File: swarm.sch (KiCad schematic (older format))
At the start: 25 parts, among them P1 USB_OTG, P2 CONN_01X05, P3 CONN_02X20, SW1 SW_PUSH, U1 LM3671MF-3.3, U2 STM32F103RETx, U3 APA102, Y1 Crystal

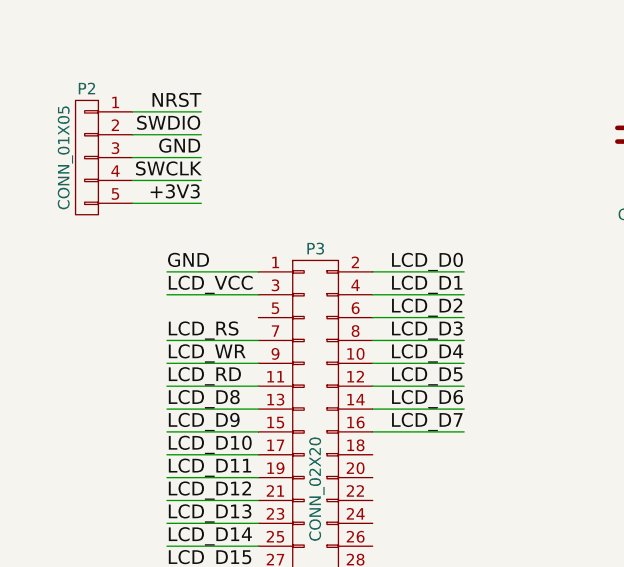
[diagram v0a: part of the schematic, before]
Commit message: Sime very important changes Connect LCD_VCC pin to VCC net, this was previously not connected Makes all elements (tracks and vias) in Power net compliant with its constraints
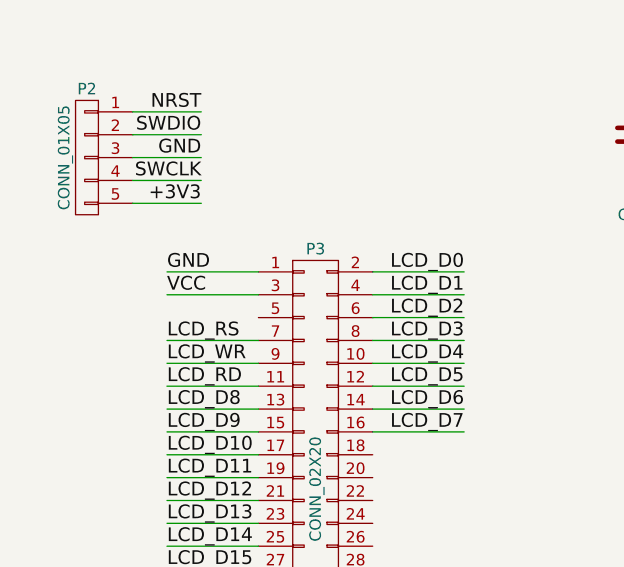
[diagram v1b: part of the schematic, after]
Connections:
- net LCD_VCC is gone; now on net VCC: P3.3 (P3)
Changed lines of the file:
@@
 GND
 Text Label 1300 5250 0    60   ~ 0
-LCD_VCC
+VCC
 Text Label 1300 5450 0    60   ~ 0
 LCD_RS

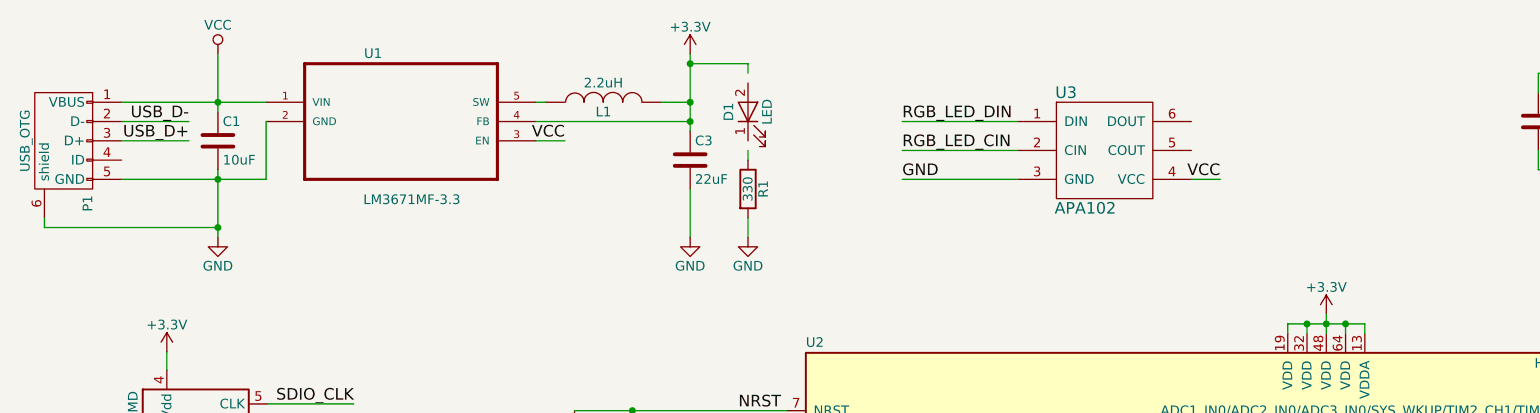
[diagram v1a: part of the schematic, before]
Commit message: Adds fuse (MF-PSMF050X) to schematic and layout
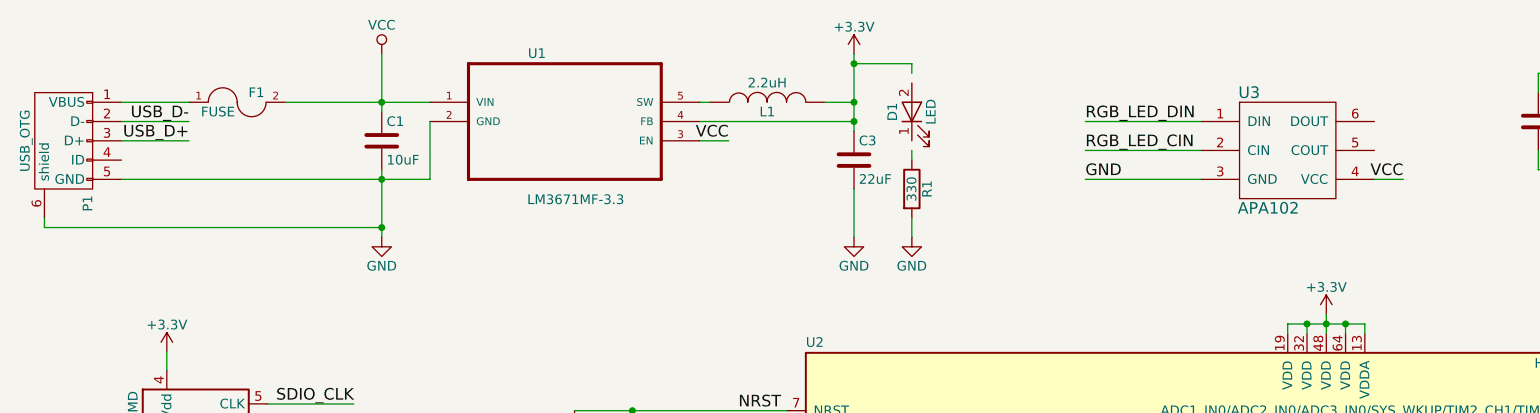
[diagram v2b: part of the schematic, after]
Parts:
- added F1: FUSE, volium:MF-PSMF050X, symbol FUSE
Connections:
- net VCC: now also F1.2; no longer P1.1 (VBUS)
- new net: F1.1, P1.1 (VBUS)
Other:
- moved on the sheet: C1, C3, D1, L1, R1, U1, U3

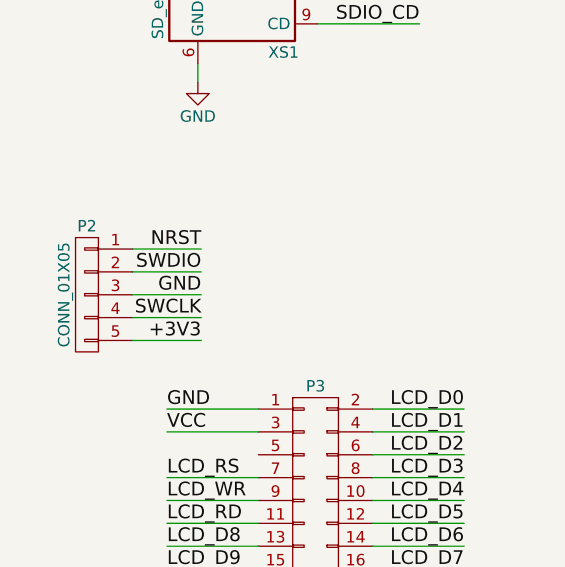
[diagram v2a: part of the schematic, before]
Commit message: Fixes pinout of debug connector, still needs to reroute
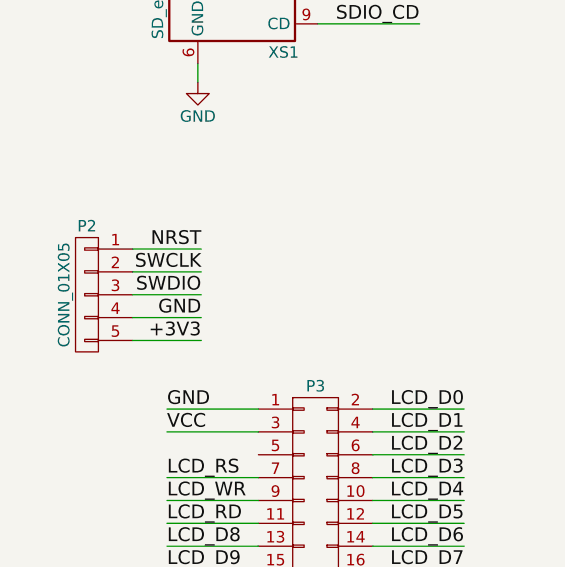
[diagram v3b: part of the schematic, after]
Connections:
- net GND: now also P2.4 (P4); no longer P2.3 (P3)
- net SWCLK: now also P2.2 (P2); no longer P2.4 (P4)
- net SWDIO: now also P2.3 (P3); no longer P2.2 (P2)
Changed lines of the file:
@@
 $EndComp
 Text Label 1450 4550 2    60   ~ 0
+SWCLK
+Text Label 1450 4650 2    60   ~ 0
 SWDIO
-Text Label 1450 4650 2    60   ~ 0
+Text Label 1450 4750 2    60   ~ 0
 GND
-Text Label 1450 4750 2    60   ~ 0
-SWCLK
 Text Label 1450 4850 2    60   ~ 0
 +3V3

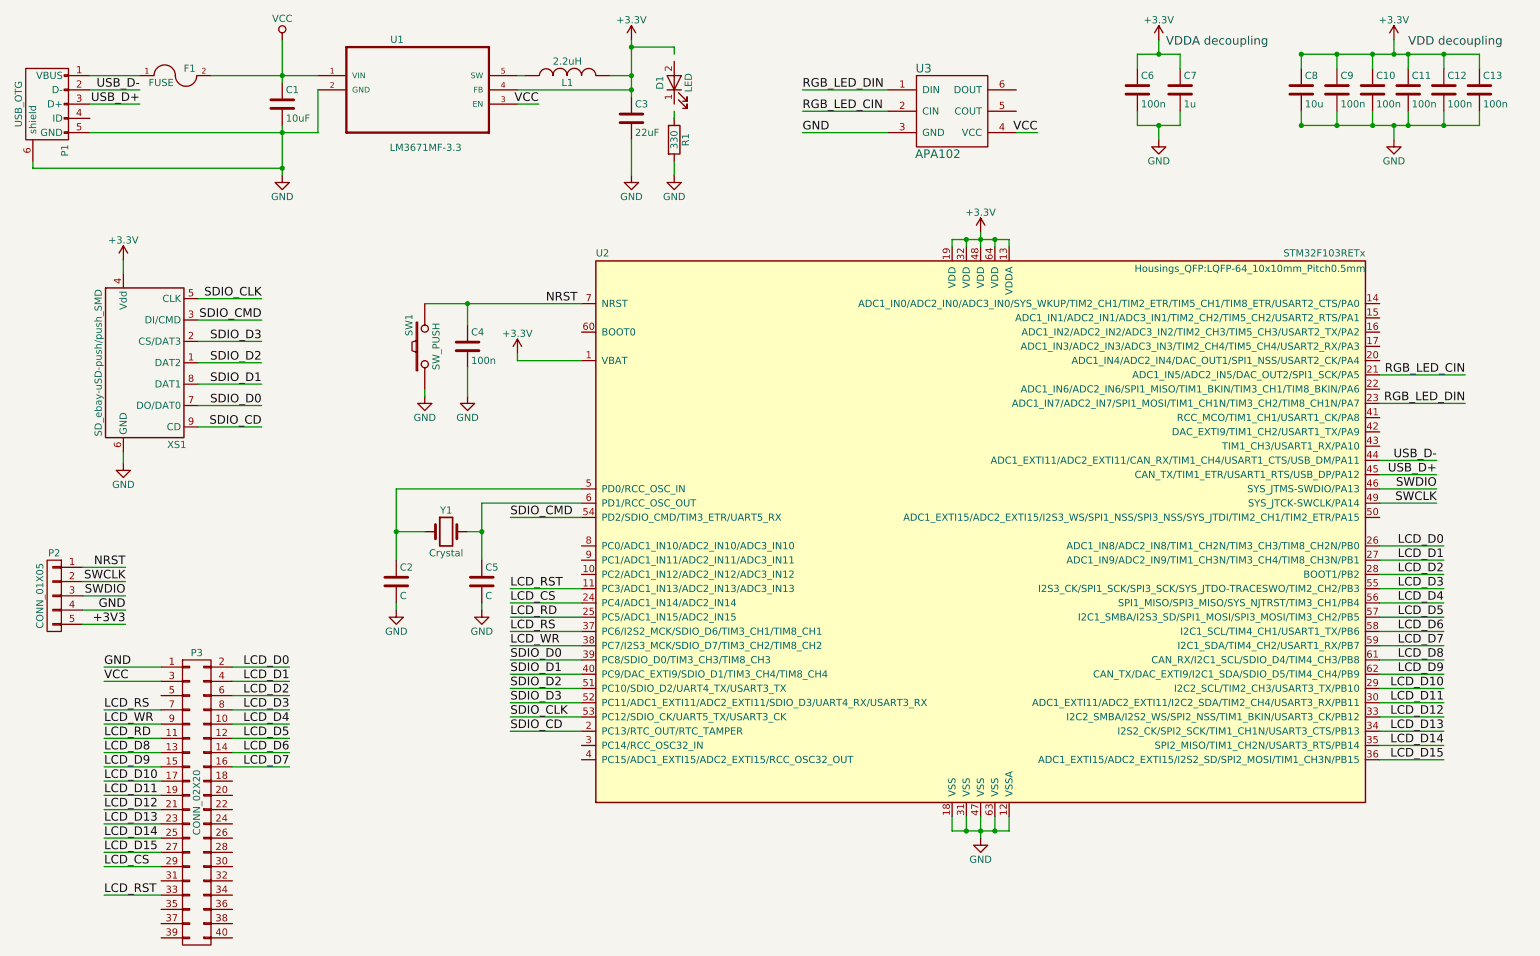
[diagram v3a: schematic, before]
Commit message: Adds LED to TIM2_CH1 (pin 50) Added PWR label, cleanup
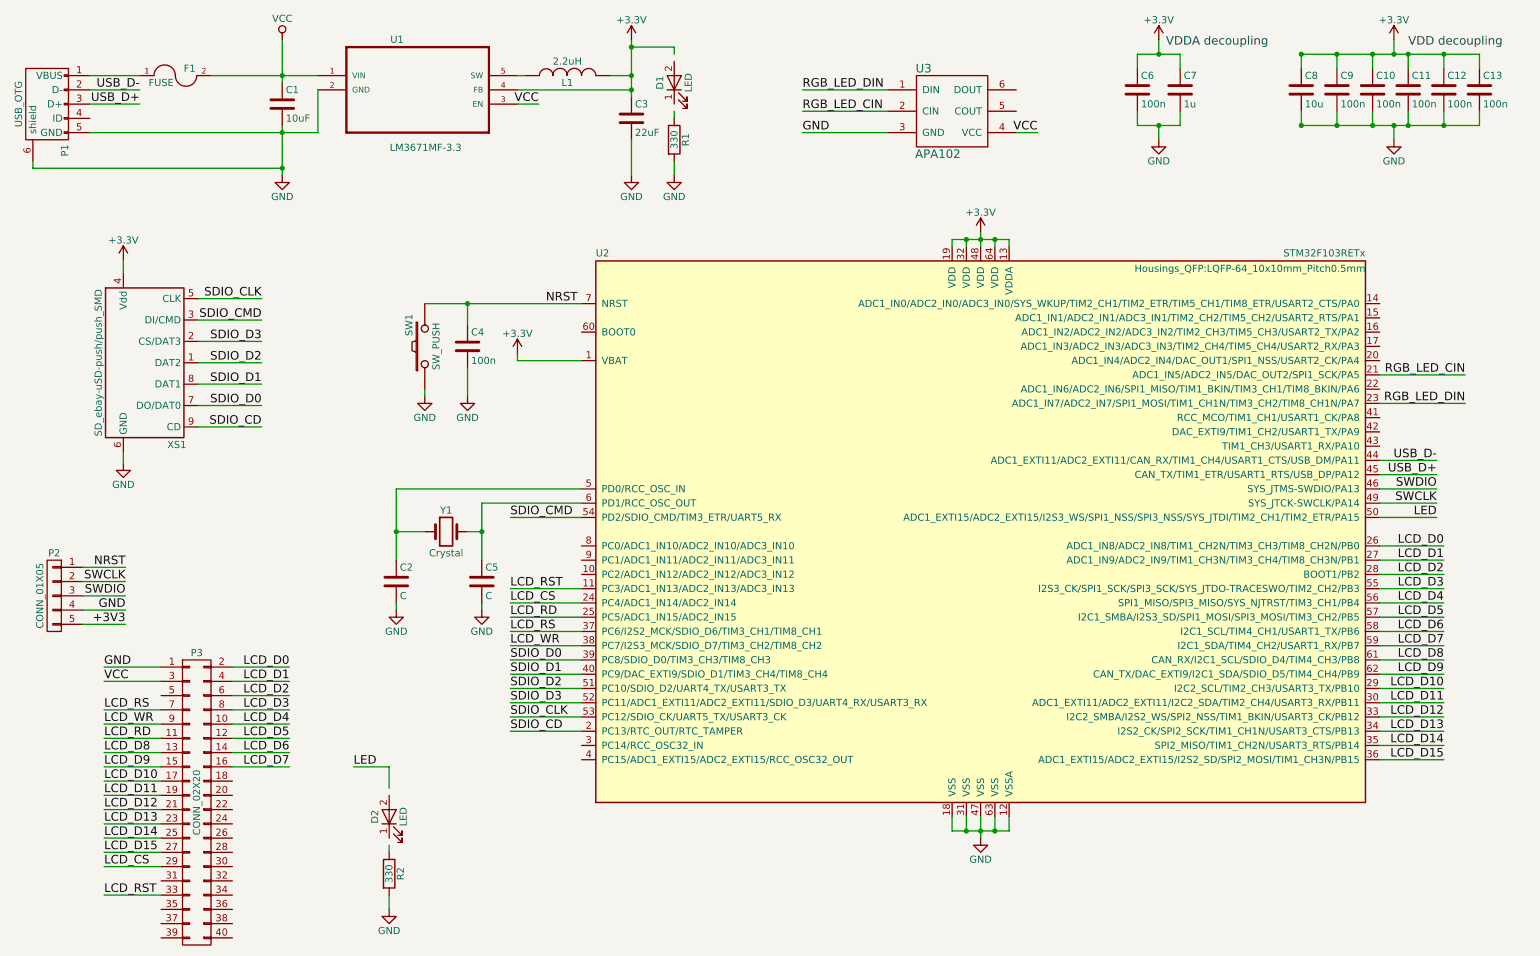
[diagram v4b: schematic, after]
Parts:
- added D2: LED, LEDs:LED_0805, symbol LED
- added R2: 330, Resistors_SMD:R_0805, symbol R
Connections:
- net GND: now also R2.2
- net LED: now reaches U2.50 (ADC1_EXTI15/ADC2_EXTI15/I2S3_WS/SPI1_NSS/SPI3_NSS/SYS_JTDI/TIM2_CH1/TIM2_ETR/PA15)
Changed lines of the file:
@@
 Wire Wire Line
 	1200 1000 1550 1000
+Text Label 10650 4100 2    60   ~ 0
+LED
+$Comp
+L LED D2
+U 1 1 5855C677
+P 3300 6200
+F 0 "D2" H 3300 6300 50  0000 C CNN
+F 1 "LED" H 3300 6100 50  0000 C CNN
+F 2 "LEDs:LED_0805" H 3300 6200 50  0001 C CNN
+F 3 "" H 3300 6200 50  0000 C CNN
+	1    3300 6200
+	0    -1   -1   0
+$EndComp
+$Comp
+L GND #PWR019
+U 1 1 5855C67D
+P 3300 6850
+F 0 "#PWR019" H 3300 6600 50  0001 C CNN
+F 1 "GND" H 3300 6700 50  0000 C CNN
+F 2 "" H 3300 6850 50  0000 C CNN
+F 3 "" H 3300 6850 50  0000 C CNN
+	1    3300 6850
+	1    0    0    -1
+$EndComp
+$Comp
+L R R2
+U 1 1 5855C683
+P 3300 6600
+F 0 "R2" V 3380 6600 50  0000 C CNN
+F 1 "330" V 3300 6600 50  0000 C CNN
+F 2 "Resistors_SMD:R_0805" V 3230 6600 50  0001 C CNN
+F 3 "" H 3300 6600 50  0000 C CNN
+	1    3300 6600
+	1    0    0    -1
+$EndComp
+Wire Wire Line
+	3300 6400 3300 6450
+Wire Wire Line
+	3300 6750 3300 6850
+Wire Wire Line
+	3300 6000 3300 5850
+Wire Wire Line
+	3300 5850 3050 5850
+Text Label 3050 5850 0    60   ~ 0
+LED
+Wire Wire Line
+	10250 4100 10650 4100
 $EndSCHEMATC

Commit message: Updates after upgrading to KiCAD 4.0.5 Updated schematic components to new libraries Cleaned up some tracks in layout
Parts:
- F1: symbol FUSE -> Polyfuse
- L1: symbol INDUCTOR -> L
- SW1: symbol SW_PUSH -> SW_Push
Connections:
- net +3V3: now also D1.2 (A)
- net LED: now also D2.2 (A)
- net at D1.1 (K): now also R1.1
- net at D2.1 (K): now also R2.1
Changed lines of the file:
@@
 LIBS:stm32
 LIBS:volium
+LIBS:switches
 LIBS:swarm-cache
 EELAYER 25 0
@@
 $EndComp
 $Comp
-L SW_PUSH SW1
+L SW_Push SW1
 U 1 1 5813891F
 P 3550 2900
@@
 $EndComp
 $Comp
-L INDUCTOR L1
+L L L1
 U 1 1 5840B3E5
 P 4550 1000
@@
 SDIO_CD
 $Comp
-L FUSE F1
+L Polyfuse F1
 U 1 1 584EF4C4
 P 1800 1000
-F 0 "F1" H 1900 1050 50  0000 C CNN
-F 1 "FUSE" H 1700 950 50  0000 C CNN
+F 0 "F1" V 1900 1050 50  0000 C CNN
+F 1 "FUSE" V 1700 950 50  0000 C CNN
 F 2 "volium:MF-PSMF050X" H 1800 1000 50  0001 C CNN
 F 3 "" H 1800 1000 50  0000 C CNN
 	1    1800 1000
-	1    0    0    -1
+	0    -1   -1   0
 $EndComp
 Wire Wire Line
@@
 Connection ~ 7450 6300
 Wire Wire Line
-	7450 6200 7450 6350
+	7450 6200 7450 6300
+Wire Wire Line
+	7450 6300 7450 6350
 Connection ~ 7450 2150
 Wire Wire Line
@@
 Connection ~ 7550 2150
 Wire Wire Line
-	7450 2100 7450 2200
+	7450 2100 7450 2150
+Wire Wire Line
+	7450 2150 7450 2200
 Wire Wire Line
 	7350 2200 7350 2150
@@
 	7250 2150 7250 2200
 Wire Wire Line
-	7250 6300 7650 6300
+	7250 6300 7350 6300
+Wire Wire Line
+	7350 6300 7450 6300
+Wire Wire Line
+	7450 6300 7550 6300
+Wire Wire Line
+	7550 6300 7650 6300
 Wire Wire Line
 	7650 6300 7650 6200
@@
 Connection ~ 10350 850
 Wire Wire Line
-	9700 1350 10950 1350
+	9700 1350 9950 1350
+Wire Wire Line
+	9950 1350 10200 1350
+Wire Wire Line
+	10200 1350 10350 1350
+Wire Wire Line
+	10350 1350 10450 1350
+Wire Wire Line
+	10450 1350 10700 1350
+Wire Wire Line
+	10700 1350 10950 1350
 Wire Wire Line
 	10700 1350 10700 1250
@@
 	3850 3050 3850 3250
 Wire Wire Line
-	3550 2600 4650 2600
+	3550 2600 3850 2600
+Wire Wire Line
+	3850 2600 4650 2600
 Wire Wire Line
 	3850 2600 3850 2750
 Wire Wire Line
-	3550 3250 3550 3200
+	3550 3250 3550 3100
 Connection ~ 3850 2600
 Wire Wire Line
 	4650 3900 3350 3900
 Wire Wire Line
-	3350 3900 3350 4400
+	3350 3900 3350 4200
+Wire Wire Line
+	3350 4200 3350 4400
 Wire Wire Line
 	3350 4200 3550 4200
@@
 	3850 4200 3950 4200
 Wire Wire Line
-	3950 4000 3950 4400
+	3950 4000 3950 4200
+Wire Wire Line
+	3950 4200 3950 4400
 Wire Wire Line
 	3950 4750 3950 4700
@@
 Connection ~ 2550 1000
 Wire Wire Line
-	2550 1350 2550 1700
-Wire Wire Line
-	1200 1400 2800 1400
-Wire Wire Line
-	5000 750  5000 1150
+	2550 1350 2550 1400
+Wire Wire Line
+	2550 1400 2550 1650
+Wire Wire Line
+	2550 1650 2550 1700
+Wire Wire Line
+	1200 1400 2550 1400
+Wire Wire Line
+	2550 1400 2800 1400
+Wire Wire Line
+	5000 750  5000 800
+Wire Wire Line
+	5000 800  5000 1000
+Wire Wire Line
+	5000 1000 5000 1100
+Wire Wire Line
+	5000 1100 5000 1150
 Wire Wire Line
 	4200 1100 5000 1100
 Wire Wire Line
-	2550 750  2550 1050
+	2550 750  2550 1000
+Wire Wire Line
+	2550 1000 2550 1050
 Connection ~ 5000 1000
 Wire Wire Line
@@
 	4200 1200 4350 1200
 Wire Wire Line
-	2050 1000 2800 1000
+	1950 1000 2550 1000
+Wire Wire Line
+	2550 1000 2800 1000
 Connection ~ 5000 1100
 Wire Wire Line
-	4850 1000 5000 1000
-Wire Wire Line
-	5300 800  5300 850
+	4700 1000 5000 1000
+Wire Wire Line
+	5300 800  5300 900
 Wire Wire Line
 	5000 800  5300 800
 Connection ~ 5000 800
 Wire Wire Line
-	5300 1250 5300 1300
+	5300 1200 5300 1300
 Wire Wire Line
 	5300 1600 5300 1700
 Connection ~ 2550 1400
 Wire Wire Line
-	4200 1000 4250 1000
+	4200 1000 4400 1000
 Wire Wire Line
 	10250 4300 10700 4300
@@
 	8550 1250 8550 1350
 Wire Wire Line
-	8550 1350 8850 1350
+	8550 1350 8700 1350
+Wire Wire Line
+	8700 1350 8850 1350
 Wire Wire Line
 	8850 1350 8850 1250
@@
 	8850 850  8850 950
 Wire Wire Line
-	8550 850  8850 850
+	8550 850  8700 850
+Wire Wire Line
+	8700 850  8850 850
 Wire Wire Line
 	8700 850  8700 750
@@
 	10250 3300 10850 3300
 Wire Wire Line
-	9700 850  10950 850
+	9700 850  9950 850
+Wire Wire Line
+	9950 850  10200 850
+Wire Wire Line
+	10200 850  10350 850
+Wire Wire Line
+	10350 850  10450 850
+Wire Wire Line
+	10450 850  10700 850
+Wire Wire Line
+	10700 850  10950 850
 Wire Wire Line
 	6800 1400 6200 1400
@@
 	10950 1350 10950 1250
 Wire Wire Line
-	7250 2150 7650 2150
+	7250 2150 7350 2150
+Wire Wire Line
+	7350 2150 7450 2150
+Wire Wire Line
+	7450 2150 7550 2150
+Wire Wire Line
+	7550 2150 7650 2150
 Wire Wire Line
 	7650 2150 7650 2200
@@
 	4650 5600 4150 5600
 Wire Wire Line
-	1200 1000 1550 1000
+	1200 1000 1650 1000
 Text Label 10650 4100 2    60   ~ 0
 LED
@@
 $EndComp
 Wire Wire Line
-	3300 6400 3300 6450
+	3300 6350 3300 6450
 Wire Wire Line
 	3300 6750 3300 6850
 Wire Wire Line
-	3300 6000 3300 5850
+	3300 6050 3300 5850
 Wire Wire Line
 	3300 5850 3050 5850
@@
 Wire Wire Line
 	10250 4100 10650 4100
+Wire Wire Line
+	3550 2600 3550 2700
 $EndSCHEMATC

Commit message: Minor changes
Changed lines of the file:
@@
 Connection ~ 7450 6300
 Wire Wire Line
-	7450 6200 7450 6300
-Wire Wire Line
-	7450 6300 7450 6350
+	7450 6200 7450 6350
 Connection ~ 7450 2150
 Wire Wire Line
@@
 Connection ~ 7550 2150
 Wire Wire Line
-	7450 2100 7450 2150
-Wire Wire Line
-	7450 2150 7450 2200
+	7450 2100 7450 2200
 Wire Wire Line
 	7350 2200 7350 2150
@@
 	7250 2150 7250 2200
 Wire Wire Line
-	7250 6300 7350 6300
-Wire Wire Line
-	7350 6300 7450 6300
-Wire Wire Line
-	7450 6300 7550 6300
-Wire Wire Line
-	7550 6300 7650 6300
+	7250 6300 7650 6300
 Wire Wire Line
 	7650 6300 7650 6200
@@
 Connection ~ 10350 850
 Wire Wire Line
-	9700 1350 9950 1350
-Wire Wire Line
-	9950 1350 10200 1350
-Wire Wire Line
-	10200 1350 10350 1350
-Wire Wire Line
-	10350 1350 10450 1350
-Wire Wire Line
-	10450 1350 10700 1350
-Wire Wire Line
-	10700 1350 10950 1350
+	9700 1350 10950 1350
 Wire Wire Line
 	10700 1350 10700 1250
@@
 	3850 3050 3850 3250
 Wire Wire Line
-	3550 2600 3850 2600
-Wire Wire Line
-	3850 2600 4650 2600
+	3550 2600 4650 2600
 Wire Wire Line
 	3850 2600 3850 2750
@@
 	4650 3900 3350 3900
 Wire Wire Line
-	3350 3900 3350 4200
-Wire Wire Line
-	3350 4200 3350 4400
+	3350 3900 3350 4400
 Wire Wire Line
 	3350 4200 3550 4200
@@
 	3850 4200 3950 4200
 Wire Wire Line
-	3950 4000 3950 4200
-Wire Wire Line
-	3950 4200 3950 4400
+	3950 4000 3950 4400
 Wire Wire Line
 	3950 4750 3950 4700
@@
 Connection ~ 2550 1000
 Wire Wire Line
-	2550 1350 2550 1400
-Wire Wire Line
-	2550 1400 2550 1650
-Wire Wire Line
-	2550 1650 2550 1700
-Wire Wire Line
-	1200 1400 2550 1400
-Wire Wire Line
-	2550 1400 2800 1400
-Wire Wire Line
-	5000 750  5000 800
-Wire Wire Line
-	5000 800  5000 1000
-Wire Wire Line
-	5000 1000 5000 1100
-Wire Wire Line
-	5000 1100 5000 1150
+	2550 1350 2550 1700
+Wire Wire Line
+	1200 1400 2800 1400
+Wire Wire Line
+	5000 750  5000 1150
 Wire Wire Line
 	4200 1100 5000 1100
 Wire Wire Line
-	2550 750  2550 1000
-Wire Wire Line
-	2550 1000 2550 1050
+	2550 750  2550 1050
 Connection ~ 5000 1000
 Wire Wire Line
@@
 	4200 1200 4350 1200
 Wire Wire Line
-	1950 1000 2550 1000
-Wire Wire Line
-	2550 1000 2800 1000
+	1950 1000 2800 1000
 Connection ~ 5000 1100
 Wire Wire Line
@@
 	8550 1250 8550 1350
 Wire Wire Line
-	8550 1350 8700 1350
-Wire Wire Line
-	8700 1350 8850 1350
+	8550 1350 8850 1350
 Wire Wire Line
 	8850 1350 8850 1250
@@
 	8850 850  8850 950
 Wire Wire Line
-	8550 850  8700 850
-Wire Wire Line
-	8700 850  8850 850
+	8550 850  8850 850
 Wire Wire Line
 	8700 850  8700 750
@@
 	10250 3300 10850 3300
 Wire Wire Line
-	9700 850  9950 850
-Wire Wire Line
-	9950 850  10200 850
-Wire Wire Line
-	10200 850  10350 850
-Wire Wire Line
-	10350 850  10450 850
-Wire Wire Line
-	10450 850  10700 850
-Wire Wire Line
-	10700 850  10950 850
+	9700 850  10950 850
 Wire Wire Line
 	6800 1400 6200 1400
@@
 	10950 1350 10950 1250
 Wire Wire Line
-	7250 2150 7350 2150
-Wire Wire Line
-	7350 2150 7450 2150
-Wire Wire Line
-	7450 2150 7550 2150
-Wire Wire Line
-	7550 2150 7650 2150
+	7250 2150 7650 2150
 Wire Wire Line
 	7650 2150 7650 2200
